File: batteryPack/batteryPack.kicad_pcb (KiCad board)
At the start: 2 copper layers, 204 x 78 mm, 38 parts, among them J1 Mirco USB, J10 B1+, J11 B1-, J12 B2-, J13 B1+, J14 B1-, J15 B2+, J16 B2-, J2 B1+, J3 B1-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

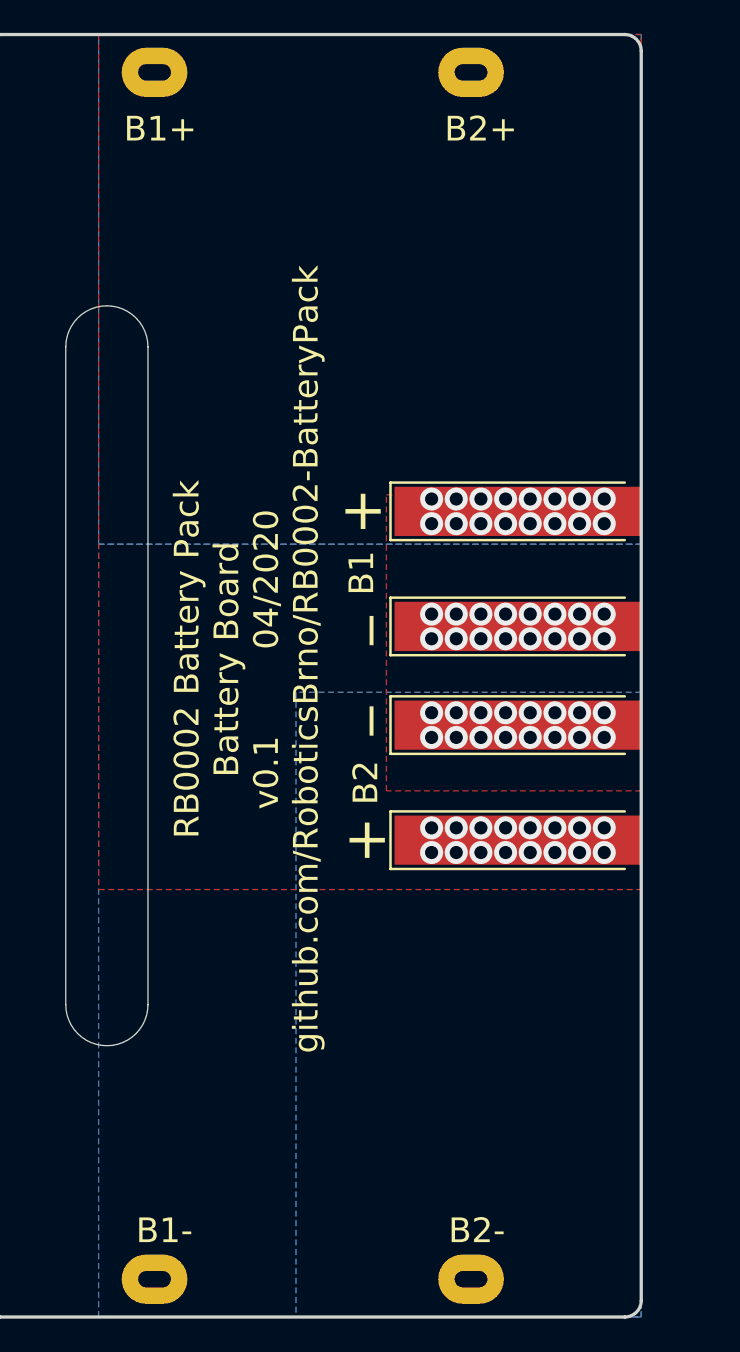
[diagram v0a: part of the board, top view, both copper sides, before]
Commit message: Swap layers on battery board
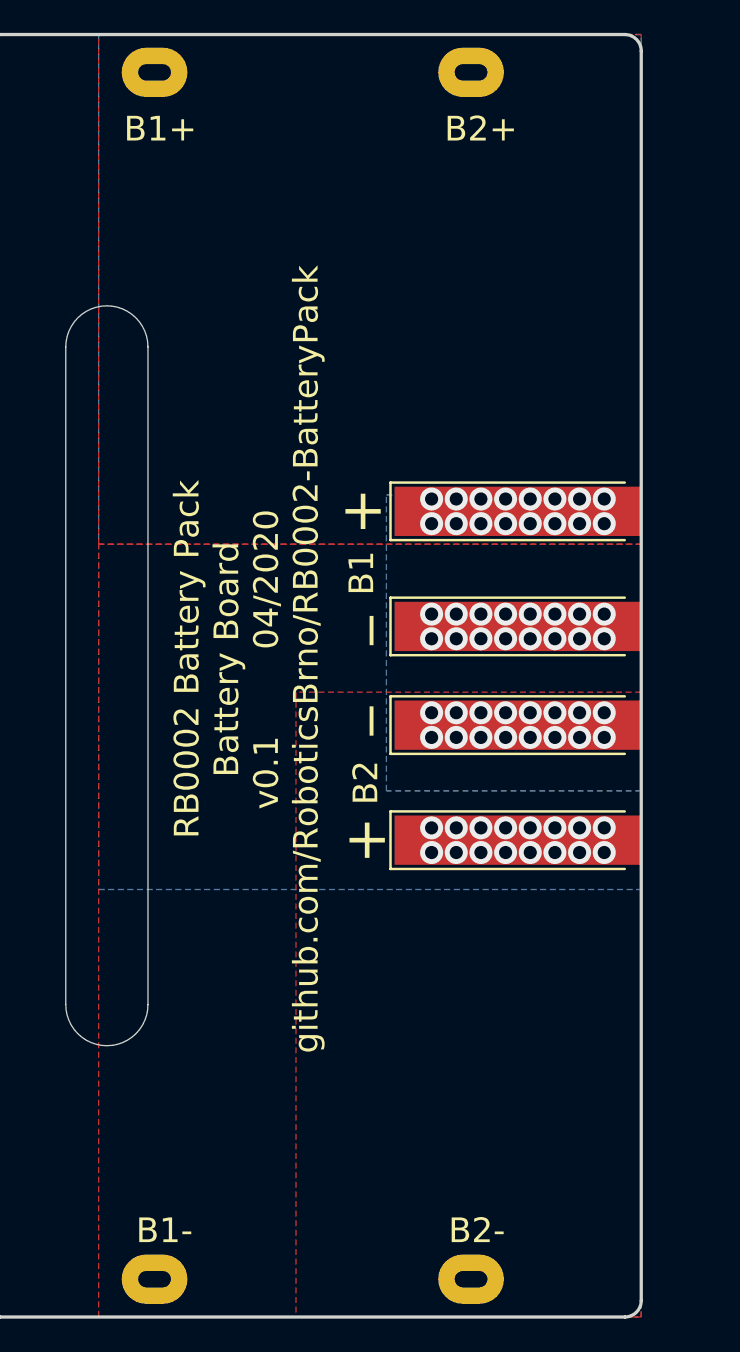
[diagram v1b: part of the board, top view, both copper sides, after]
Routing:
- added copper zone on F.Cu, net /BP_B1+
- added copper zone on F.Cu, net /BP_B1-
- added copper zone on B.Cu, net /BP_B2+
- added copper zone on F.Cu, net /BP_B2-
- removed copper zone on B.Cu, net /BP_B1+
- removed copper zone on B.Cu, net /BP_B1-
- removed copper zone on F.Cu, net /BP_B2+
- removed copper zone on B.Cu, net /BP_B2-
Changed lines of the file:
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@@
     (user_trace_width 2)
     (trace_clearance 0.2)
-    (zone_clearance 0.5)
+    (zone_clearance 1)
     (zone_45_only no)
     (trace_min 0.2)
@@
   (segment (start 207 58) (end 206.625 58.375) (width 0.25) (layer B.Cu) (net 32))
   (segment (start 207.5 58) (end 207 58) (width 0.25) (layer B.Cu) (net 32))
-  (zone (net 28) (net_name /BP_B1+) (layer B.Cu) (hatch edge 0.508)
+  (zone (net 28) (net_name /BP_B1+) (layer F.Cu) (hatch edge 0.508)
     (priority 1)
     (connect_pads yes (clearance 1))
@@
     )
   )
-  (zone (net 27) (net_name /BP_B1-) (layer B.Cu) (hatch edge 0.508)
+  (zone (net 27) (net_name /BP_B1-) (layer F.Cu) (hatch edge 0.508)
     (priority 2)
     (connect_pads yes (clearance 1))
@@
     )
   )
-  (zone (net 26) (net_name /BP_B2-) (layer B.Cu) (hatch edge 0.508)
+  (zone (net 26) (net_name /BP_B2-) (layer F.Cu) (hatch edge 0.508)
     (priority 3)
     (connect_pads yes (clearance 1))
@@
     )
   )
-  (zone (net 25) (net_name /BP_B2+) (layer F.Cu) (hatch edge 0.508)
+  (zone (net 25) (net_name /BP_B2+) (layer B.Cu) (hatch edge 0.508)
     (priority 3)
     (connect_pads yes (clearance 1))

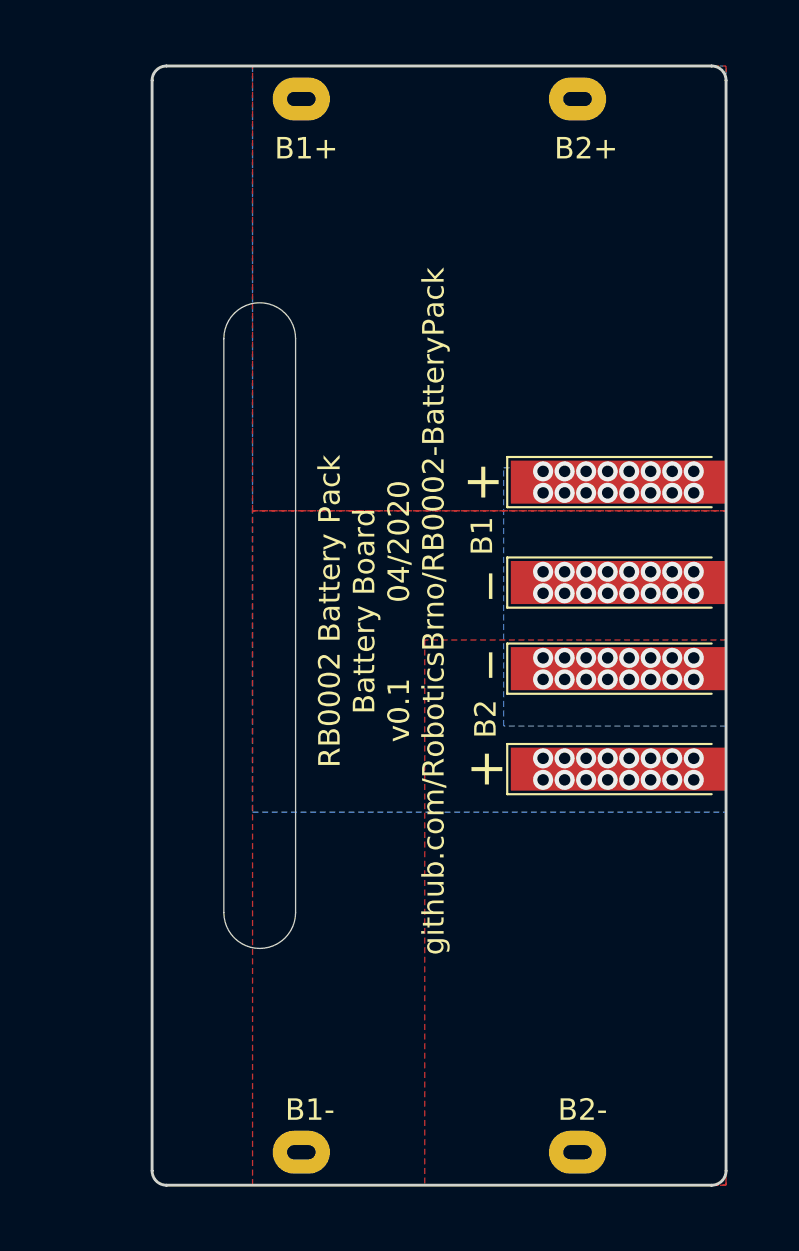
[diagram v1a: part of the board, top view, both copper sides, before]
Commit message: Add tenons and handle to the battery
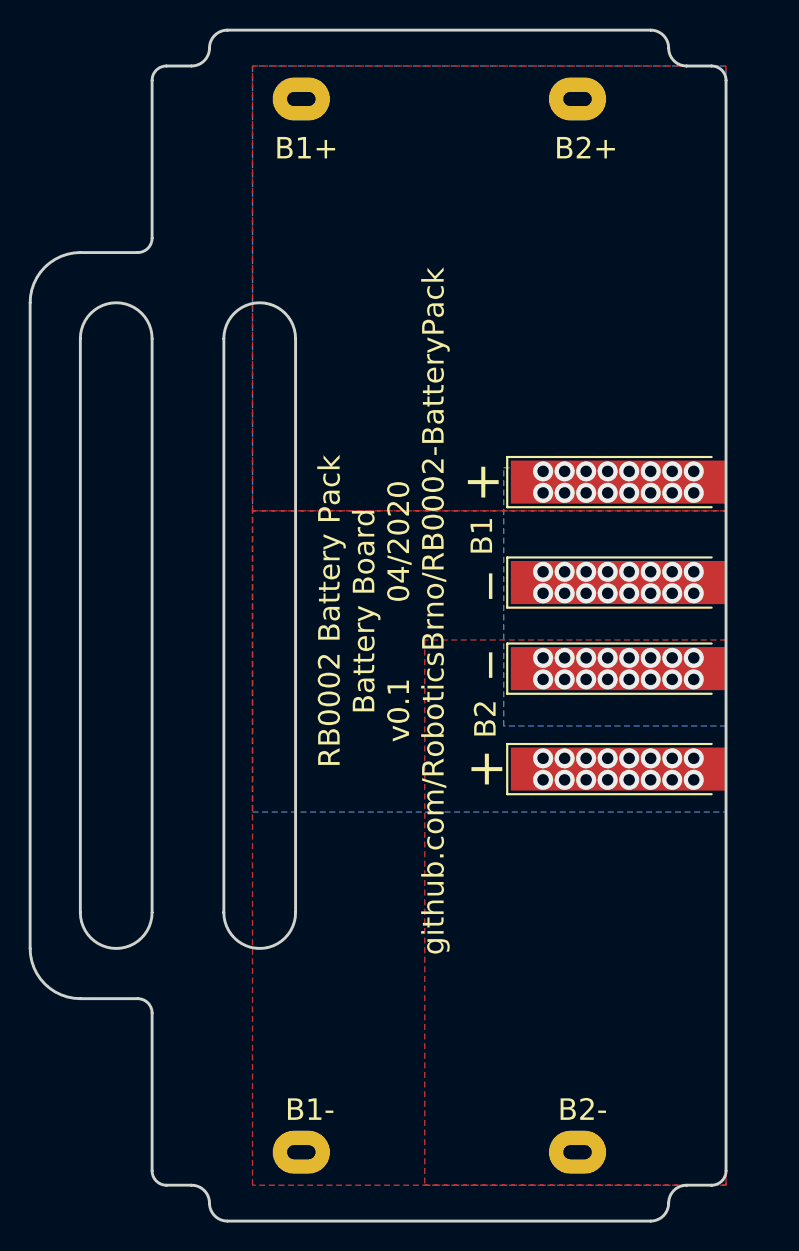
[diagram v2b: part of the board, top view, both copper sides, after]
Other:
- board size 204 x 78 mm -> 212.5 x 83 mm
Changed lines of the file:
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@@
   (general
     (thickness 1.6)
-    (drawings 107)
+    (drawings 131)
     (tracks 441)
     (zones 0)
@@
   (page A4)
   (layers
-    (0 F.Cu signal)
-    (31 B.Cu signal)
+    (0 F.Cu signal hide)
+    (31 B.Cu signal hide)
     (32 B.Adhes user)
     (33 F.Adhes user)
@@
     )
   )
-  (gr_line (start 40 50) (end 40 90) (layer Edge.Cuts) (width 0.05))
-  (gr_arc (start 37.5 50) (end 40 50) (angle -180) (layer Edge.Cuts) (width 0.05))
-  (gr_line (start 35 50) (end 35 90) (layer Edge.Cuts) (width 0.05))
-  (gr_arc (start 37.5 90) (end 35 90) (angle -180) (layer Edge.Cuts) (width 0.05))
+  (gr_line (start 31 109) (end 32.75 109) (layer Edge.Cuts) (width 0.2))
+  (gr_line (start 67.25 109) (end 69 109) (layer Edge.Cuts) (width 0.2))
+  (gr_arc (start 67.25 110.25) (end 67.25 109) (angle -90) (layer Edge.Cuts) (width 0.2))
+  (gr_arc (start 35.25 110.25) (end 34 110.25) (angle -90) (layer Edge.Cuts) (width 0.2))
+  (gr_line (start 35.25 111.5) (end 64.75 111.5) (layer Edge.Cuts) (width 0.2))
+  (gr_arc (start 64.75 110.25) (end 64.75 111.5) (angle -90) (layer Edge.Cuts) (width 0.2))
+  (gr_arc (start 32.75 110.25) (end 34 110.25) (angle -90) (layer Edge.Cuts) (width 0.2))
+  (gr_line (start 32.75 31) (end 31 31) (layer Edge.Cuts) (width 0.2))
+  (gr_line (start 69 31) (end 67.25 31) (layer Edge.Cuts) (width 0.2))
+  (gr_arc (start 35.25 29.75) (end 35.25 28.5) (angle -90) (layer Edge.Cuts) (width 0.2))
+  (gr_arc (start 32.75 29.75) (end 32.75 31) (angle -90) (layer Edge.Cuts) (width 0.2))
+  (gr_arc (start 67.25 29.75) (end 66 29.75) (angle -90) (layer Edge.Cuts) (width 0.2))
+  (gr_arc (start 64.75 29.75) (end 66 29.75) (angle -90) (layer Edge.Cuts) (width 0.2))
+  (gr_line (start 64.75 28.5) (end 35.25 28.5) (layer Edge.Cuts) (width 0.2))
+  (gr_line (start 21.5 47.5) (end 21.5 92.5) (layer Edge.Cuts) (width 0.2))
+  (gr_arc (start 25 92.5) (end 21.5 92.5) (angle -90) (layer Edge.Cuts) (width 0.2))
+  (gr_line (start 29 96) (end 25 96) (layer Edge.Cuts) (width 0.2))
+  (gr_arc (start 25 47.5) (end 25 44) (angle -90) (layer Edge.Cuts) (width 0.2))
+  (gr_line (start 29 44) (end 25 44) (layer Edge.Cuts) (width 0.2))
+  (gr_line (start 25 50) (end 25 90) (layer Edge.Cuts) (width 0.2))
+  (gr_arc (start 27.5 50) (end 30 50) (angle -180) (layer Edge.Cuts) (width 0.2))
+  (gr_arc (start 27.5 90) (end 25 90) (angle -180) (layer Edge.Cuts) (width 0.2))
+  (gr_line (start 30 50) (end 30 90) (layer Edge.Cuts) (width 0.2))
+  (gr_arc (start 29 97) (end 30 97) (angle -90) (layer Edge.Cuts) (width 0.2))
+  (gr_line (start 30 97) (end 30 108) (layer Edge.Cuts) (width 0.2))
+  (gr_arc (start 29 43) (end 29 44) (angle -90) (layer Edge.Cuts) (width 0.2))
+  (gr_line (start 30 32) (end 30 43) (layer Edge.Cuts) (width 0.2))
+  (gr_line (start 40 50) (end 40 90) (layer Edge.Cuts) (width 0.2))
+  (gr_arc (start 37.5 50) (end 40 50) (angle -180) (layer Edge.Cuts) (width 0.2))
+  (gr_line (start 35 50) (end 35 90) (layer Edge.Cuts) (width 0.2))
+  (gr_arc (start 37.5 90) (end 35 90) (angle -180) (layer Edge.Cuts) (width 0.2))
   (gr_text "github.com/RoboticsBrno/\nRB0002-BatteryPack" (at 124.5 70 270) (layer F.SilkS)
     (effects (font (size 1.3 1.3) (thickness 0.2)))
@@
   )
   (dimension 78 (width 0.3) (layer F.Fab)
-    (gr_text "78,000 mm" (at 20.550001 70 270) (layer F.Fab)
-      (effects (font (size 1 1) (thickness 0.15)))
-    )
-    (feature1 (pts (xy 31 109) (xy 21.41358 109)))
-    (feature2 (pts (xy 31 31) (xy 21.41358 31)))
-    (crossbar (pts (xy 22.000001 31) (xy 22.000001 109)))
-    (arrow1a (pts (xy 22.000001 109) (xy 21.41358 107.873496)))
-    (arrow1b (pts (xy 22.000001 109) (xy 22.586422 107.873496)))
-    (arrow2a (pts (xy 22.000001 31) (xy 21.41358 32.126504)))
-    (arrow2b (pts (xy 22.000001 31) (xy 22.586422 32.126504)))
+    (gr_text "78,000 mm" (at 13.3 70.25 270) (layer F.Fab)
+      (effects (font (size 1 1) (thickness 0.15)))
+    )
+    (feature1 (pts (xy 23.749999 109.25) (xy 14.163579 109.25)))
+    (feature2 (pts (xy 23.749999 31.25) (xy 14.163579 31.25)))
+    (crossbar (pts (xy 14.75 31.25) (xy 14.75 109.25)))
+    (arrow1a (pts (xy 14.75 109.25) (xy 14.163579 108.123496)))
+    (arrow1b (pts (xy 14.75 109.25) (xy 15.336421 108.123496)))
+    (arrow2a (pts (xy 14.75 31.25) (xy 14.163579 32.376504)))
+    (arrow2b (pts (xy 14.75 31.25) (xy 15.336421 32.376504)))
   )
   (gr_arc (start 69 32) (end 70 32) (angle -90) (layer Edge.Cuts) (width 0.2))
@@
     (effects (font (size 2 2) (thickness 0.4)))
   )
-  (gr_line (start 30 108) (end 30 32) (layer Edge.Cuts) (width 0.2))
-  (gr_line (start 69 109) (end 31 109) (layer Edge.Cuts) (width 0.2))
   (gr_line (start 70 32) (end 70 108) (layer Edge.Cuts) (width 0.2))
-  (gr_line (start 31 31) (end 69 31) (layer Edge.Cuts) (width 0.2))
   (dimension 36.25 (width 0.15) (layer F.Fab)
     (gr_text "36,250 mm" (at 254.45 70.125 270) (layer F.Fab)
